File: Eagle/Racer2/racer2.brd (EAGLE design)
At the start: 73.3 x 33 mm, 9 parts

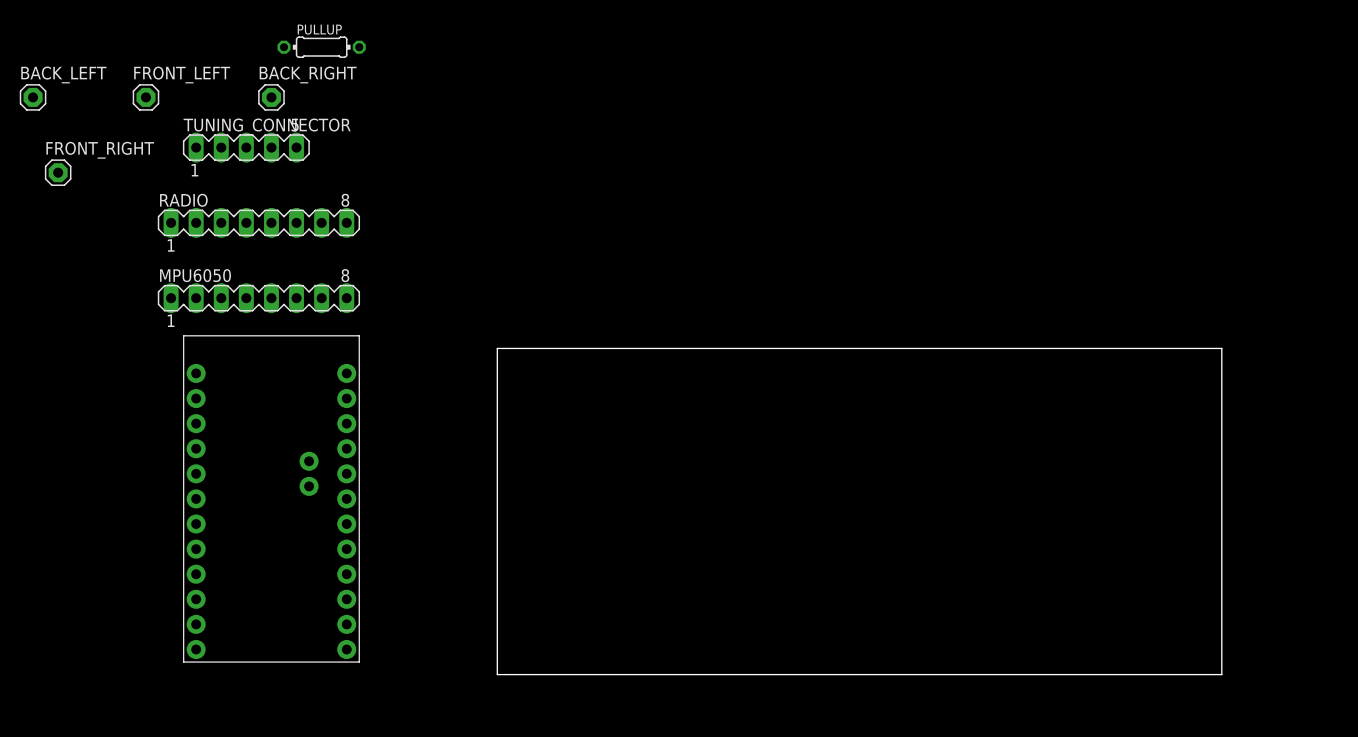
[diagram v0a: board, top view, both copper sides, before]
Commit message: Changed structure of imu code.
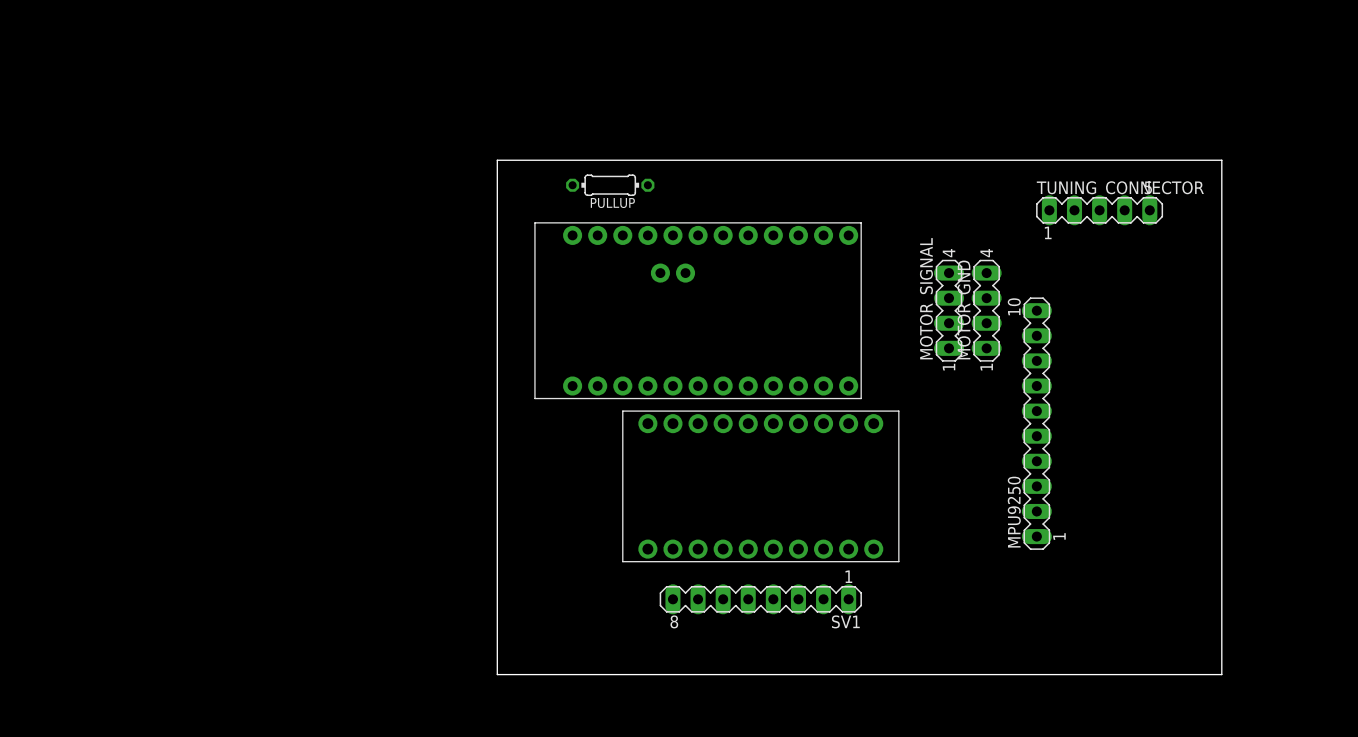
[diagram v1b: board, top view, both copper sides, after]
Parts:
- removed BACK_LEFT, BACK_RIGHT, FRONT_LEFT, FRONT_RIGHT: (no value), adafruit:1X01
- removed MPU6050, RADIO: (no value), con-lstb:MA08-1
- added MOTOR_GND, MOTOR_SIGNAL: (no value), con-lstb:MA04-1
- added MPU9250: (no value), con-lstb:MA10-1
- added SV1: (no value), con-lstb:MA08-1
- added U$2: LEVELSHIFT_8CH, quadcopter_comp:LEVELSHIFT_8CH
- U$1: device SAMD21_mini:SAMD21G-MINI -> quadcopter_comp:SAMD21G-MINI
- moved TUNING_CONNECTOR 86.6 mm to (61.0, 47.0)
- moved U$1 63.1 mm to (20.3, 36.8), turned to 90 degrees
- moved PULLUP 32.4 mm to (11.4, 49.5), turned to 180 degrees
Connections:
- new net N$10: MOTOR_SIGNAL.2, U$1.12
- new net N$11: SV1.4, U$2.B4
- new net N$12: MOTOR_SIGNAL.4, U$1.10
- new net N$13: SV1.5, U$2.B5
- new net N$14: SV1.6, U$2.B6
- new net N$18: U$1.VCC, U$2.VCCA
- new net N$19: U$1.4, U$2.A6
- new net N$20: U$1.5, U$2.A5
- new net N$21: U$1.6, U$2.A4
- new net N$22: U$1.7, U$2.A3
- new net N$23: U$1.8, U$2.A2
- new net N$24: U$1.9, U$2.A1
- new net N$9: MOTOR_SIGNAL.1, U$1.13
- net 5V: now also MPU9250.10, SV1.7, U$2.VCCB; no longer MPU6050.8, RADIO.8
- net GND2: now also SV1.8, U$2.GND; no longer RADIO.7
- net N$1: now also MPU9250.7; no longer MPU6050.5
- net N$2: now also MPU9250.8; no longer MPU6050.6
- net N$3: now also MOTOR_GND.1, MOTOR_GND.2, MOTOR_GND.3, MOTOR_GND.4, MPU9250.4, MPU9250.9; no longer MPU6050.2, MPU6050.7
- net N$4: now also SV1.1, U$2.B1; no longer U$1.10
- net N$5: now also MOTOR_SIGNAL.3
- net N$6: now also SV1.2, U$2.B2; no longer U$1.12
- net N$7: now also SV1.3, U$2.B3; no longer U$1.13
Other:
- board size 73.3 x 33 mm -> 73.3 x 52.1 mm

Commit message: Updated.
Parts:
- removed MOTOR_GND, MOTOR_SIGNAL: (no value), con-lstb:MA04-1
- removed MPU9250: (no value), con-lstb:MA10-1
- removed SV1: (no value), con-lstb:MA08-1
- added POWER: (no value), con-lstb:MA03-1
- added U$10, U$6, U$7, U$8, U$9: BRIDGE, quadcopter_comp:BRIDGE
- added U$3: FS_RADIO, quadcopter_comp:FS_RADIO
- added U$4: MPU9250, quadcopter_comp:MPU9250
- added U$5: MOTOR_HEADER, quadcopter_comp:MOTOR_HEADER
- U$1: value SAMD21G_MINI -> NANO; device quadcopter_comp:SAMD21G-MINI -> quadcopter_comp:NANO
- U$2: value LEVELSHIFT_8CH -> BUTTON_PULLUP; device quadcopter_comp:LEVELSHIFT_8CH -> quadcopter_comp:BUTTON_PULLUP
- moved PULLUP 73.1 mm to (80.0, 24.1), turned to 270 degrees
- moved TUNING_CONNECTOR 28.2 mm to (75.6, 22.9), turned to 270 degrees
- moved U$1 27.4 mm to (22.2, 9.53), turned to 270 degrees
- moved U$2 26.9 mm to (52.1, 27.9), turned to 180 degrees
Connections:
- removed net GND2: SV1.8, TUNING_CONNECTOR.4, U$1.GND2, U$2.GND
- removed net N$20: U$1.5, U$2.A5
- removed net N$21: U$1.6, U$2.A4
- removed net N$22: U$1.7, U$2.A3
- removed net N$23: U$1.8, U$2.A2
- removed net N$24: U$1.9, U$2.A1
- new net GND: POWER.2, TUNING_CONNECTOR.4, U$1.GND, U$1.GND2, U$2.B, U$3.GND, U$4.AD0, U$4.GND, U$5.GND1, U$5.GND2, U$5.GND3, U$5.GND4
- new net N$15: U$3.VCC, U$9.A
- new net N$17: U$1.A4, U$6.A
- new net N$8: U$1.D6, U$3.CH5
- net 5V: now also POWER.3, U$1.5V, U$10.B, U$9.B; no longer MPU9250.10, SV1.7, U$1.VIN, U$2.VCCB
- net N$1: now also U$1.D12, U$8.A; no longer MPU9250.7, TUNING_CONNECTOR.3, U$1.SDA
- net N$10: now also U$1.D8, U$5.FL; no longer MOTOR_SIGNAL.2, U$1.12
- net N$11: now also U$1.D9, U$5.FR; no longer SV1.4, U$2.B4
- net N$12: now also U$1.D10, U$5.BL; no longer MOTOR_SIGNAL.4, U$1.10
- net N$13: now also U$1.D11, U$5.BR; no longer SV1.5, U$2.B5
- net N$14: now also U$2.A, U$3.BAT; no longer SV1.6, U$2.B6
- net N$16: now also U$8.B; no longer U$1.2
- net N$18: now also TUNING_CONNECTOR.2, U$4.SCL, U$7.B; no longer U$1.VCC, U$2.VCCA
- net N$19: now also U$10.A, U$4.VCC; no longer U$1.4, U$2.A6
- net N$2: now also U$1.A5, U$7.A; no longer MPU9250.8, TUNING_CONNECTOR.2, U$1.SCL
- net N$3: now also TUNING_CONNECTOR.3, U$4.SDA, U$6.B; no longer MOTOR_GND.1, MOTOR_GND.2, MOTOR_GND.3, MOTOR_GND.4, MPU9250.4, MPU9250.9, U$1.GND
- net N$4: now also U$1.D3, U$3.CH2; no longer SV1.1, U$2.B1
- net N$5: now also U$1.D2, U$3.CH1; no longer MOTOR_SIGNAL.3, U$1.11
- net N$6: now also U$1.D4, U$3.CH3; no longer SV1.2, U$2.B2
- net N$7: now also U$1.D5, U$3.CH4; no longer SV1.3, U$2.B3
- net N$9: now also U$1.D7, U$3.CH6; no longer MOTOR_SIGNAL.1, U$1.13
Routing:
- net GND: track 0.00 -> 195.2 mm
- net 5V: track 0.00 -> 75.3 mm
- net N$15: track 0.00 -> 60.3 mm
- net N$2: track 0.00 -> 51.6 mm
- net N$17: track 0.00 -> 50.3 mm
- net N$16: track 0.00 -> 49.6 mm
- net N$13: track 0.00 -> 46.9 mm
- net N$12: track 0.00 -> 43.3 mm
- net N$11: track 0.00 -> 39.7 mm
- net N$10: track 0.00 -> 37.5 mm
- net N$14: track 0.00 -> 29.3 mm
- net N$1: track 0.00 -> 26.4 mm
- net N$9: track 0.00 -> 21.1 mm
- net N$8: track 0.00 -> 17.5 mm
- net N$3: track 0.00 -> 15.9 mm
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- added copper zone on layer 16, net GND
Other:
- board size 73.3 x 52.1 mm -> 85.1 x 38.1 mm
- board text added: "16-08-29"
- board text added: "JOHAN ISAKSSON"

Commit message: Started on new Explorer code.
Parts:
- added PULLUP1: (no value), eagle-ltspice:0204/7
- added U$11: ATMEGA328P, quadcopter_comp:ATMEGA328P
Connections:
- new net N$20: PULLUP1.2, U$11.PC6
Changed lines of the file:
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@@
 <element name="U$9" library="quadcopter_comp" package="BRIDGE" value="BRIDGE" x="26.035" y="5.08" rot="R90"/>
 <element name="U$10" library="quadcopter_comp" package="BRIDGE" value="BRIDGE" x="71.12" y="21.59"/>
+<element name="U$11" library="quadcopter_comp" package="ATMEGA328P" value="ATMEGA328P" x="-5.715" y="17.78"/>
+<element name="PULLUP1" library="eagle-ltspice" package="0204/7" value="" x="-5.715" y="-3.175">
+<attribute name="SPICEMODEL" value="NONE" x="-5.715" y="-3.175" size="1.778" layer="27" display="off"/>
+<attribute name="SPICEPREFIX" value="R" x="-5.715" y="-3.175" size="1.778" layer="27" display="off"/>
+</element>
 </elements>
 <signals>
@@
 <wire x1="68.58" y1="30.48" x2="71.12" y2="27.94" width="0.6096" layer="16"/>
 </signal>
+<signal name="N$20">
+<contactref element="PULLUP1" pad="2"/>
+<contactref element="U$11" pad="PC6"/>
+<wire x1="-1.905" y1="-3.175" x2="-9.525" y2="34.29" width="0" layer="19" extent="1-1"/>
+</signal>
 </signals>
